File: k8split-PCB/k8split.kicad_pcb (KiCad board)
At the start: 2 copper layers, 397.3 x 124 mm, 245 parts, among them J1 AVR-ISP-6, J2 AVR-ISP-6, J3 Breakaway_Tabs, J4 Breakaway_Tabs, J5 Breakaway_Tabs, J6 Breakaway_Tabs, J7 Breakaway_Tabs, J8 Breakaway_Tabs, J9 Breakaway_Tabs, SW1 SW_Push, SW2 SW_Push, U1 ATmega32U4-AU, U2 ATmega32U4-AU, Y1 16MHz, Y2 16MHz

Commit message: pcb update for rev0.2
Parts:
- removed C10: 1uF, Capacitor_SMD:C_0603_1608Metric
- removed C11, C16, C5: 0.1uF, Capacitor_SMD:C_0603_1608Metric
- removed C14: 10uF, Capacitor_SMD:C_0603_1608Metric
- removed C8, C9: 22pF, Capacitor_SMD:C_0603_1608Metric
- removed the G*** at (128.5, 121.9)
- removed the G*** at (136.1, 121.9)
- removed R2, R67: 10k, Resistor_SMD:R_0603_1608Metric
- removed R5, R6: 22, Resistor_SMD:R_0603_1608Metric
- removed SW2: SW_Push, locallib:SKQGADE010
- removed U2: ATmega32U4-AU, Package_QFP:TQFP-44_10x10mm_P0.8mm
- removed USB2: USB_A_SMT, locallib:CUI_UJ2-AH-4-SMT
- removed Y2: 16MHz, Crystal:Crystal_SMD_3225-4Pin_3.2x2.5mm
- added G***: LOGO, locallib:cklogopro_10_10, F.Cu at (145.1, 74.2)
- added G***: LOGO, cad:r, B.Cu at (152.6, 37.7)
- added G***: LOGO, cad:l, B.Cu at (115.6, 38.2)
- added J11: DE15_Socket_HighDensity_MountingHoles, Connector_Dsub:DSUB-15-HD_Socket_Horizontal_P2.29x1.90mm_EdgePinOffset3.03mm_Housed_MountingHolesOffset4.94mm, F.Cu at (-47.6, 24.2)
- added J12: DE15_Socket_HighDensity_MountingHoles, Connector_Dsub:DSUB-15-HD_Socket_Horizontal_P2.29x1.90mm_EdgePinOffset3.03mm_Housed_MountingHolesOffset4.94mm, F.Cu at (303.3, 24.2)
- D1, D10, D11, D12, D13, D14, D15, D16, D17, D18, D19, D2, D20, D21, D22, D23, D24, D25, D26, D27, D28, D29, D3, D30, D31, D32, D33, D34, D35, D36, D37, D38, D39, D4, D40, D41, D42, D43, D44, D45, D46, D47, D48, D49, D5, D50, D51, D52, D53, D54, D55, D56, D57, D58, D59, D6, D60, D61, D62, D63, D64, D65, D66, D67, D68, D69, D7, D70, D71, D72, D73, D74, D75, D76, D77, D78, D79, D8, D80, D81, D82, D83, D84, D85, D86, D87, D88, D89, D9, D90, D91, D92, D93, D94, D95, D96: footprint Diode_SMD:D_SOD-123 -> Diode_THT:D_A-405_P10.16mm_Horizontal
- G*** (x2): moved to B.Cu
- J1, J2: value AVR-ISP-6 -> DE15_Socket_HighDensity_MountingHoles; footprint random-keyboard-parts:Reset_Pretty -> Connector_Dsub:DSUB-15-HD_Socket_Horizontal_P2.29x1.90mm_EdgePinOffset3.03mm_Housed_MountingHolesOffset4.94mm
- MX1, MX10, MX11, MX12, MX13, MX14, MX15, MX16, MX17, MX18, MX19, MX2, MX20, MX21, MX22, MX23, MX25, MX26, MX27, MX28, MX29, MX31, MX32, MX33, MX34, MX35, MX36, MX37, MX38, MX39, MX40, MX41, MX42, MX43, MX44, MX45, MX46, MX47, MX48, MX49, MX50, MX51, MX52, MX53, MX54, MX55, MX56, MX57, MX58, MX59, MX61, MX62, MX63, MX64, MX65, MX67, MX68, MX69, MX7, MX70, MX71, MX72, MX73, MX74, MX75, MX76, MX77, MX78, MX79, MX8, MX80, MX81, MX82, MX83, MX84, MX85, MX86, MX87, MX88, MX89, MX9, MX90, MX91: footprint MX_Only:MXOnly-1U-NoLED -> PCM_marbastlib-xp-choc:SW_choc_v2_1u
- MX24, MX66: footprint MX_Only:MXOnly-1.25U-NoLED -> PCM_marbastlib-xp-choc:SW_choc_v2_1.25u
- MX3, MX6, MX93, MX96: footprint MX_Only:MXOnly-1.5U-NoLED -> PCM_marbastlib-xp-choc:SW_choc_v2_1.5u
- MX30, MX5, MX60, MX94: footprint MX_Only:MXOnly-2.25U-NoLED -> locallib:SW_choc_v2_2.25u
- MX4: footprint MX_Only:MXOnly-1.75U-NoLED -> PCM_marbastlib-xp-choc:SW_choc_v2_1.75u
- MX92: footprint MX_Only:MXOnly-2U-NoLED -> locallib:SW_choc_v2_2u
- MX95: footprint MX_Only:MXOnly-2.75U-NoLED -> locallib:SW_choc_v2_2.75u
- Y1: footprint Crystal:Crystal_SMD_3225-4Pin_3.2x2.5mm -> Crystal:Crystal_HC49-4H_Vertical; moved to F.Cu
- moved G*** 194.4 mm to (-53.9, 28.2), turned to 180 degrees
- moved USB1 183.5 mm to (130.9, 73.3), turned to 180 degrees
- moved R3 176.8 mm to (128.5, 68.4), turned to -90 degrees
- moved R4 172.8 mm to (126.4, 68.4), turned to -90 degrees
- moved G*** 166.2 mm to (317.1, 27.7), turned to 180 degrees
- moved C4 139.0 mm to (137.1, 56.2), turned to 90 degrees
- moved R25 133.3 mm to (131.1, 41.7), turned to -90 degrees
- moved C15 130.0 mm to (121.1, 44.7)
- moved C3 126.5 mm to (125.1, 63.7)
- moved U1 126.1 mm to (127.0, 52.4), turned to 90 degrees
- moved C7 124.3 mm to (133.6, 62.2)
- moved C6 107.8 mm to (116.6, 55.7)
- moved Y1 105.5 mm to (110.6, 55.6), turned to 90 degrees
- moved C1 102.1 mm to (104.6, 50.7), turned to 180 degrees
- moved C2 99.2 mm to (104.6, 55.7), turned to 180 degrees
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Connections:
- C1 pad 1: Net-(C1-Pad1) -> Net-(U1-XTAL1)
- C2 pad 1: Net-(C2-Pad1) -> Net-(U1-XTAL2)
- D1 pad 1: ROW0 -> ROW0-L
- D10 pad 1: ROW3 -> ROW3-L
- D11 pad 1: ROW4 -> ROW4-L
- D12 pad 1: ROW5 -> ROW5-L
- D13 pad 1: ROW0 -> ROW0-L
- D14 pad 1: ROW1 -> ROW1-L
- D15 pad 1: ROW2 -> ROW2-L
- D16 pad 1: ROW3 -> ROW3-L
- D17 pad 1: ROW4 -> ROW4-L
- D18 pad 1: ROW5 -> ROW5-L
- D19 pad 1: ROW0 -> ROW0-L
- D2 pad 1: ROW1 -> ROW1-L
- D20 pad 1: ROW1 -> ROW1-L
- D21 pad 1: ROW2 -> ROW2-L
- D22 pad 1: ROW3 -> ROW3-L
- D23 pad 1: ROW4 -> ROW4-L
- D24 pad 1: ROW5 -> ROW5-L
- D25 pad 1: ROW0 -> ROW0-L
- D26 pad 1: ROW1 -> ROW1-L
- D27 pad 1: ROW2 -> ROW2-L
- D28 pad 1: ROW3 -> ROW3-L
- D29 pad 1: ROW4 -> ROW4-L
- D3 pad 1: ROW2 -> ROW2-L
- D30 pad 1: ROW5 -> ROW5-L
- D31 pad 1: ROW0 -> ROW0-L
- D32 pad 1: ROW1 -> ROW1-L
- D33 pad 1: ROW2 -> ROW2-L
- D34 pad 1: ROW3 -> ROW3-L
- D35 pad 1: ROW4 -> ROW4-L
- D36 pad 1: ROW5 -> ROW5-L
- D37 pad 1: ROW0 -> ROW0-L
- D38 pad 1: ROW1 -> ROW1-L
- D39 pad 1: ROW2 -> ROW2-L
- D4 pad 1: ROW3 -> ROW3-L
- D40 pad 1: ROW3 -> ROW3-L
- D41 pad 1: ROW4 -> ROW4-L
- D42 pad 1: ROW5 -> ROW5-L
- D43 pad 1: ROW0 -> ROW0-L
- D44 pad 1: ROW1 -> ROW1-L
- D45 pad 1: ROW2 -> ROW2-L
- D46 pad 1: ROW3 -> ROW3-L
- D47 pad 1: ROW4 -> ROW4-L
- D48 pad 1: ROW5 -> ROW5-L
- D5 pad 1: ROW4 -> ROW4-L
- D6 pad 1: ROW5 -> ROW5-L
- D7 pad 1: ROW0 -> ROW0-L
- D8 pad 1: ROW1 -> ROW1-L
- D9 pad 1: ROW2 -> ROW2-L
- J1 pad 1: MISO -> ROW0
- J1 pad 2: +5V -> ROW1
- J1 pad 3: SCK -> ROW2
- J1 pad 4: MOSI -> ROW3
- J1 pad 5: RESET -> ROW4
- J1 pad 6: GND -> ROW5
- J2 pad 1: MISO-R -> ROW0
- J2 pad 2: +5VA -> ROW1
- J2 pad 3: SCK-R -> ROW2
- J2 pad 4: MOSI-R -> ROW3
- J2 pad 5: RESET-R -> ROW4
- J2 pad 6: GNDA -> ROW5
- MX1 pad 1: COL0 -> COL0-L
- MX10 pad 1: COL1 -> COL1-L
- MX11 pad 1: COL1 -> COL1-L
- MX12 pad 1: COL1 -> COL1-L
- MX13 pad 1: COL2 -> COL2-L
- MX14 pad 1: COL2 -> COL2-L
- MX15 pad 1: COL2 -> COL2-L
- MX16 pad 1: COL2 -> COL2-L
- MX17 pad 1: COL2 -> COL2-L
- MX18 pad 1: COL2 -> COL2-L
- MX19 pad 1: COL3 -> COL3-L
- MX2 pad 1: COL0 -> COL0-L
- MX20 pad 1: COL3 -> COL3-L
- MX21 pad 1: COL3 -> COL3-L
- MX22 pad 1: COL3 -> COL3-L
- MX23 pad 1: COL3 -> COL3-L
- MX24 pad 1: COL3 -> COL3-L
- MX25 pad 1: COL4 -> COL4-L
- MX26 pad 1: COL4 -> COL4-L
- MX27 pad 1: COL4 -> COL4-L
- MX28 pad 1: COL4 -> COL4-L
- MX29 pad 1: COL4 -> COL4-L
- MX3 pad 1: COL0 -> COL0-L
- MX30 pad 1: COL4 -> COL4-L
- MX31 pad 1: COL5 -> COL5-L
- MX32 pad 1: COL5 -> COL5-L
- MX33 pad 1: COL5 -> COL5-L
- MX34 pad 1: COL5 -> COL5-L
- MX35 pad 1: COL5 -> COL5-L
- MX36 pad 1: COL5 -> COL5-L
- MX37 pad 1: COL6 -> COL6-L
- MX38 pad 1: COL6 -> COL6-L
- MX39 pad 1: COL6 -> COL6-L
- MX4 pad 1: COL0 -> COL0-L
- MX40 pad 1: COL6 -> COL6-L
- MX41 pad 1: COL6 -> COL6-L
- MX42 pad 1: COL6 -> COL6-L
- MX43 pad 1: COL7 -> COL7-L
- MX44 pad 1: COL7 -> COL7-L
- MX45 pad 1: COL7 -> COL7-L
- MX46 pad 1: COL7 -> COL7-L
- MX47 pad 1: COL7 -> COL7-L
- MX48 pad 1: COL7 -> COL7-L
- MX5 pad 1: COL0 -> COL0-L
- MX6 pad 1: COL0 -> COL0-L
- MX7 pad 1: COL1 -> COL1-L
- MX8 pad 1: COL1 -> COL1-L
- MX9 pad 1: COL1 -> COL1-L
- U1 pad 1: Net-(U1-Pad1) -> unconnected-(U1-PE6-Pad1)
- U1 pad 10: MOSI -> COL2
- U1 pad 11: MISO -> COL3
- U1 pad 12: ROW5 -> COL7
- U1 pad 16: Net-(C2-Pad1) -> Net-(U1-XTAL2)
- U1 pad 17: Net-(C1-Pad1) -> Net-(U1-XTAL1)
- U1 pad 18: ROW4 -> ROW0
- U1 pad 19: ROW3 -> ROW1
- U1 pad 21: ROW1 -> ROW3
- U1 pad 22: ROW0 -> ROW5
- U1 pad 25: COL7 -> ROW4
- U1 pad 26: COL6 -> COL14
- U1 pad 27: COL5 -> COL15
- U1 pad 29: COL3 -> COL5
- U1 pad 30: COL2 -> COL6
- U1 pad 31: COL1 -> COL12
- U1 pad 32: COL0 -> COL13
- U1 pad 36: Net-(U1-Pad36) -> COL11
- U1 pad 37: Net-(U1-Pad37) -> COL10
- U1 pad 38: Net-(U1-Pad38) -> COL9
- U1 pad 39: Net-(U1-Pad39) -> COL8
- U1 pad 40: Net-(U1-Pad40) -> unconnected-(U1-PF1-Pad40)
- U1 pad 41: Net-(U1-Pad41) -> unconnected-(U1-PF0-Pad41)
- U1 pad 42: Net-(U1-Pad42) -> unconnected-(U1-AREF-Pad42)
- U1 pad 8: Net-(U1-Pad8) -> COL0
- U1 pad 9: SCK -> COL1
- Y1 pad 1: Net-(C1-Pad1) -> Net-(U1-XTAL2)
- Y1 pad 2: GND -> Net-(U1-XTAL1)
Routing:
- net COL6-L: track 0.00 -> 406.8 mm
- net COL5-L: track 0.00 -> 382.9 mm
- net ROW4-L: track 0.00 -> 379.8 mm
- net ROW3-L: track 0.00 -> 355.5 mm
- net COL4-L: track 0.00 -> 340.4 mm
- net +5VA: track 340.3 -> 0.00 mm, vias 6 -> 0
- net ROW2-L: track 0.00 -> 333.9 mm
- net ROW5-L: track 0.00 -> 319.8 mm
- net ROW1-L: track 0.00 -> 314.4 mm
- net COL4-R: track 187.6 -> 467.0 mm, vias 1 -> 0
- net ROW5-R: track 194.4 -> 455.4 mm
- net R-D+: track 255.7 -> 0.00 mm
- net R-D-: track 254.0 -> 0.00 mm
- net COL7-L: track 0.00 -> 240.8 mm
- net +5V: track 336.3 -> 102.9 mm, vias 5 -> 4
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- removed copper zone on B.Cu, net GNDA
- removed copper zone on F.Cu, net GNDA
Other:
- board size 397.3 x 124 mm -> 397.3 x 128.1 mm
- net class Default removed
- net class POWER removed
- board text added: "COL0"
- board text added: "COL1"
- board text added: "COL10"
- board text added: "COL11"
- board text added: "COL12"
- board text added: "COL13"
- board text added: "COL14"
- board text added: "COL15"
- board text added: "COL2"
- board text added: "COL3"
- board text added: "COL4"
- board text added: "COL5"
- board text added: "COL6"
- board text added: "COL7"
- board text added: "COL8"
- board text added: "COL9"
- board text added: "K 8 S P L I T REV0.2"
- board text added: "ROW0"
- board text added: "ROW1"
- board text added: "ROW2"
- board text added: "ROW3"
- board text added: "ROW4"
- board text added: "ROW5"
- board text added: "rev 0.2"
- board text removed: "K 8 S P L I T REV0.1"
- board text removed: "initial print"
- board text removed: "might contain corona proceed with caution"
- board text removed: "rev 0.1"

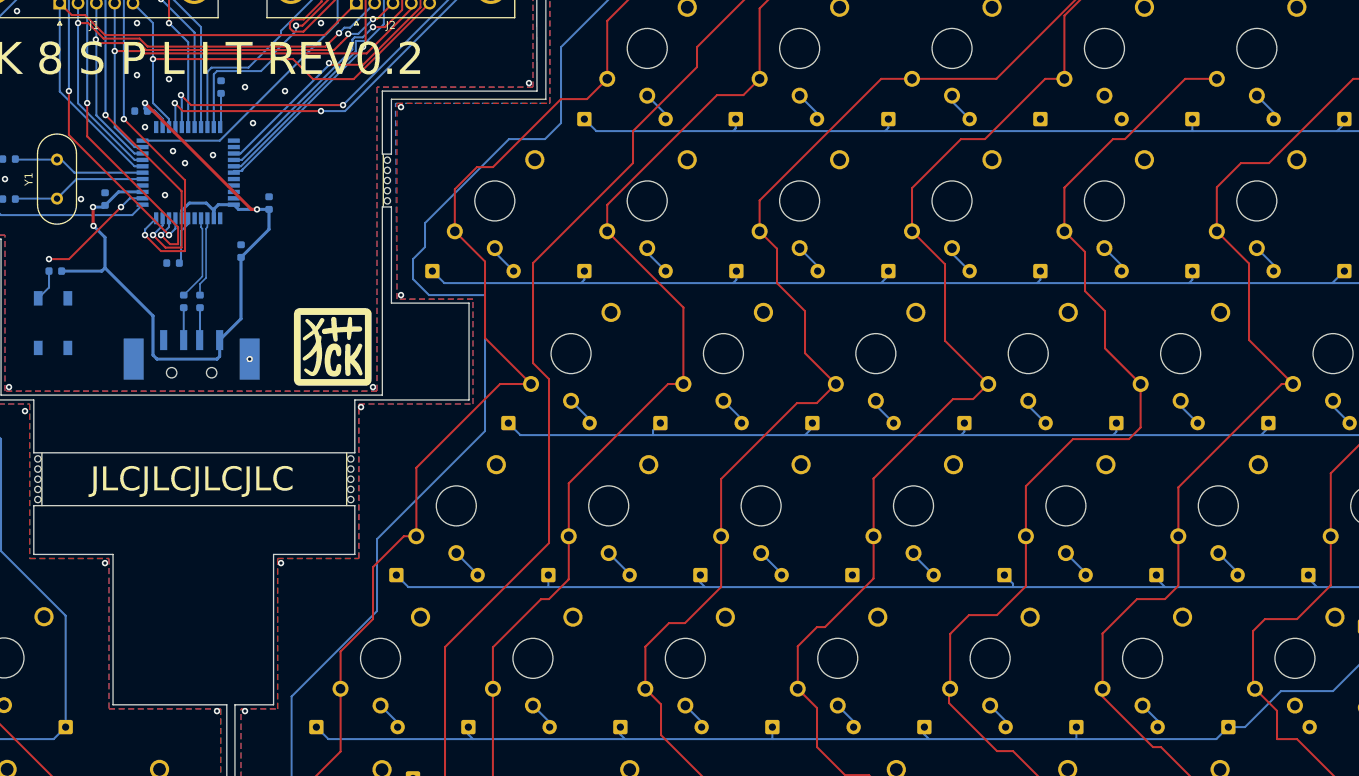
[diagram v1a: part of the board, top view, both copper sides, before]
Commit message: last minute drc fixes
- unconnected row pins
- unconnected keys
- unconnected reset
- unconnected vcc
- moved around decoupling caps a bit
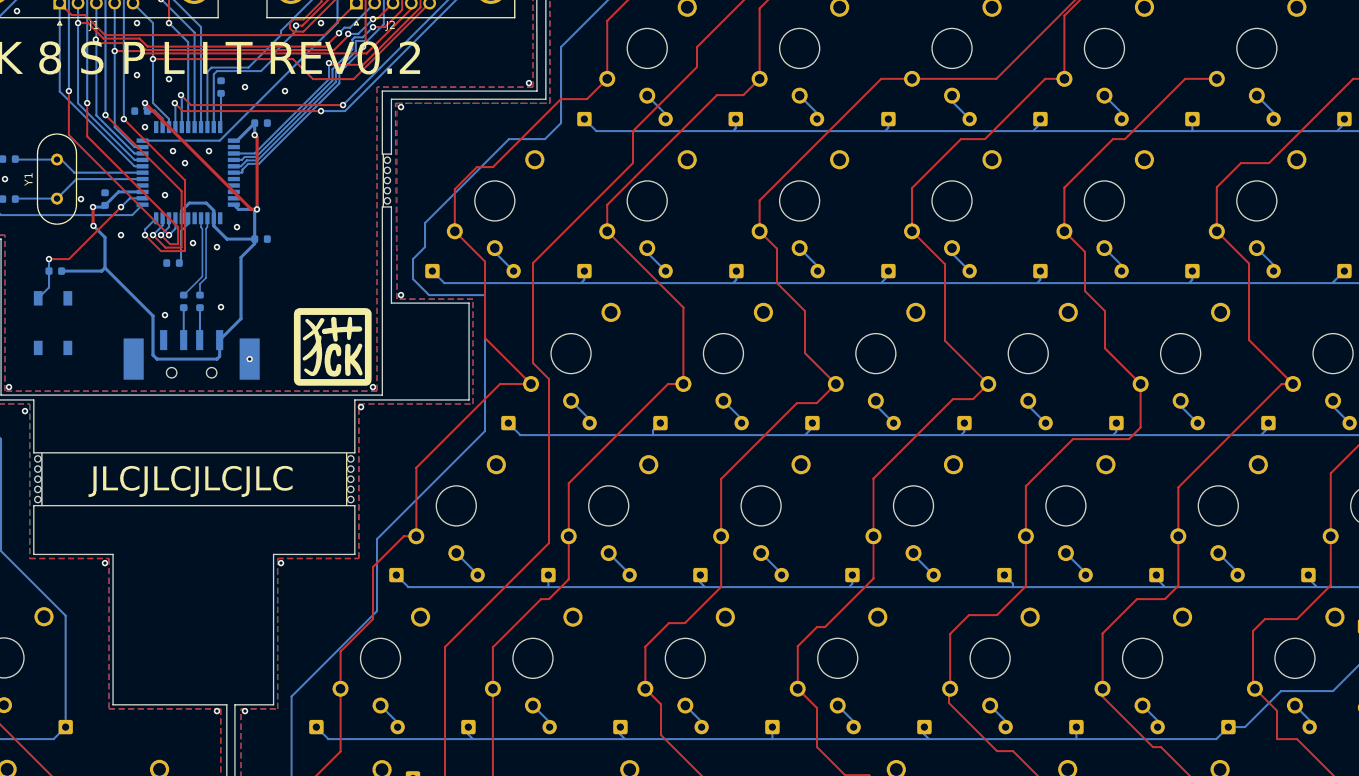
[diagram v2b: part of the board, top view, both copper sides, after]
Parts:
- moved C4 10.0 mm to (136.1, 46.2), turned to 0 degrees
- moved C7 2.92 mm to (136.1, 60.7), turned to 0 degrees
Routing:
- net +5V: track 102.9 -> 118.1 mm, vias 4 -> 5
- net Net-(D67-A): track 0.00 -> 3.82 mm
- net Net-(D89-A): track 0.00 -> 3.46 mm
- net ROW0-R: track 166.7 -> 168.6 mm
- net ROW3-R: track 257.2 -> 258.8 mm
- net RESET: track 18.8 -> 20.3 mm
- net COL11: track 33.6 -> 34.7 mm
- net COL10: track 32.3 -> 33.1 mm
- net COL9: track 31.4 -> 32.2 mm
- net COL8: track 30.5 -> 31.3 mm
- net GND: vias 41 -> 46
